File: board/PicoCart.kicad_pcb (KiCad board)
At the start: 2 copper layers, 99.8 x 99.5 mm, 29 parts, among them J1 MSX Bus (Odd-Even), J2 Micro_SD_Card, J3 UART, J4 DEBUG, J5 MSX Debug, J6 Pico Debug, J7 Ground Pins, J8 Ground Pins, J9 Edge Connector, U1 LD1117S33TR_SOT223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

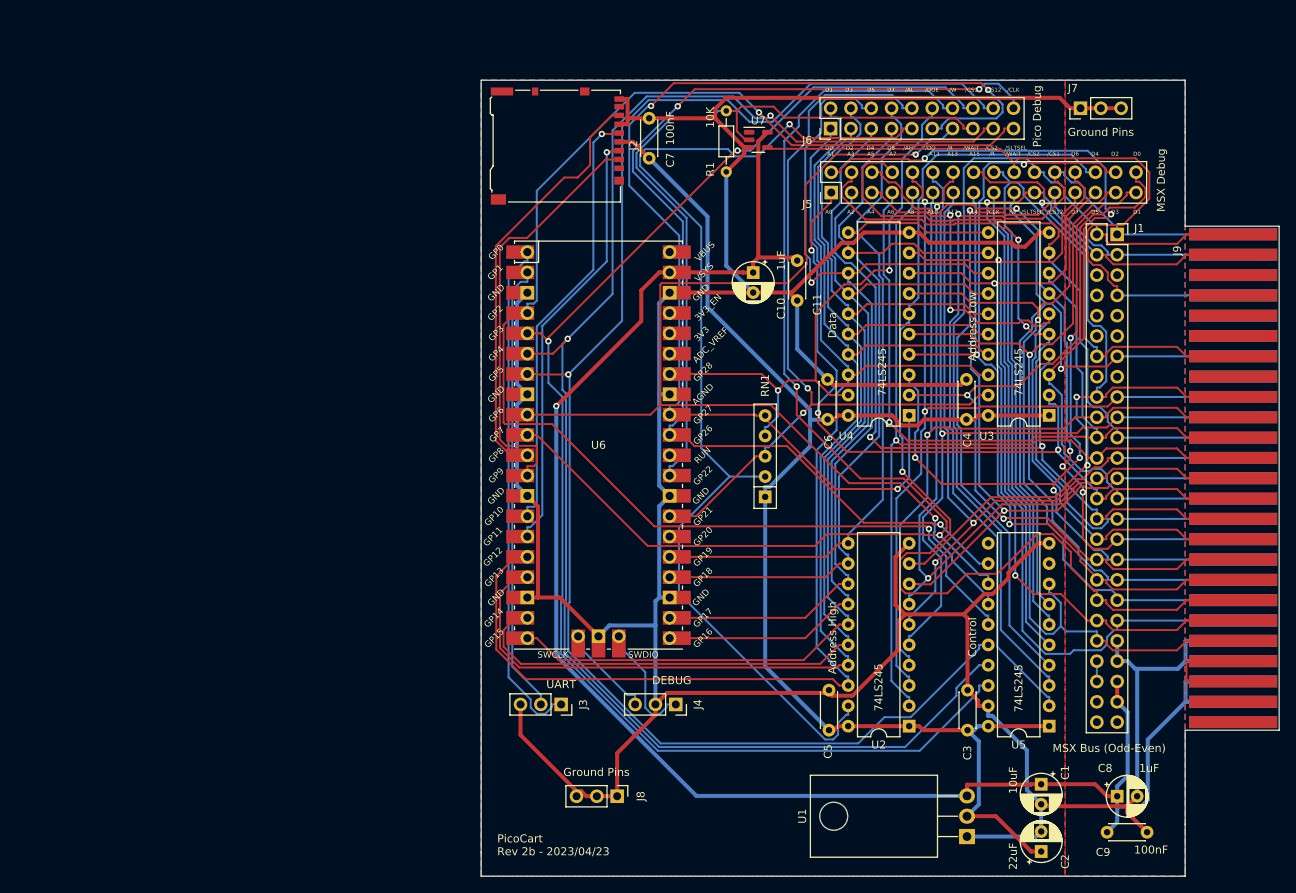
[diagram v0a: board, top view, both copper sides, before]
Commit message: Debug Board Design
Created a Debug board so that I can test the Main Pico logic against a
more controllable set of signals, rather than the MSX which provides a
very short window of usability
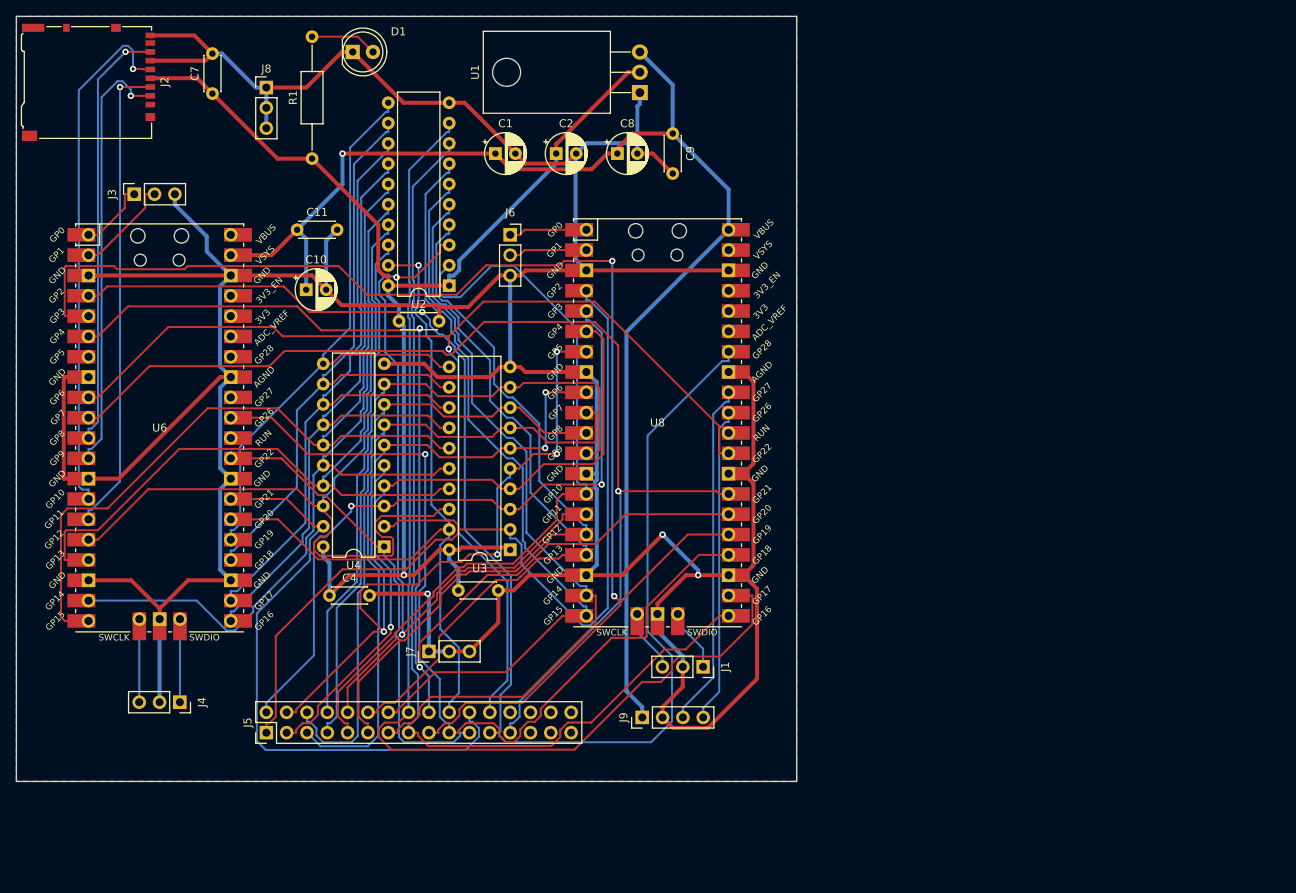
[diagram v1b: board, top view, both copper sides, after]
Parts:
- removed C6: 100nF, Capacitor_THT:C_Disc_D4.3mm_W1.9mm_P5.00mm
- removed RN1: 10K, Resistor_THT:R_Array_SIP5
- removed U5: 74LS245, Package_DIP:DIP-20_W7.62mm
- removed U7: SN74LV1T34DBV, Package_TO_SOT_SMD:SOT-23-5
- added D1: LED, LED_THT:LED_D5.0mm, F.Cu at (91.4, 37.5)
- added U8: Pico, Library:RPi_Pico_SMD_TH, F.Cu at (129.5, 83.8)
- J1: value MSX Bus (Odd-Even) -> D_DEBUG; footprint Connector_PinHeader_2.54mm:PinHeader_2x25_P2.54mm_Vertical -> Connector_PinSocket_2.54mm:PinSocket_1x03_P2.54mm_Vertical
- J6: value Pico Debug -> D_UART; footprint Connector_PinHeader_2.54mm:PinHeader_2x10_P2.54mm_Vertical -> Connector_PinSocket_2.54mm:PinSocket_1x03_P2.54mm_Vertical
- J9: value Edge Connector -> DEBUG_I2C; footprint Connector:MSX_Cartridge -> Connector_PinHeader_2.54mm:PinHeader_1x04_P2.54mm_Vertical
- R1: value 10K -> R_Small; footprint Resistor_THT:R_Axial_DIN0204_L3.6mm_D1.6mm_P7.62mm_Horizontal -> Resistor_THT:R_Axial_DIN0207_L6.3mm_D2.5mm_P15.24mm_Horizontal
- U6: footprint MCU_RaspberryPi_and_Boards:RPi_Pico_SMD_TH -> Library:RPi_Pico_SMD_TH
- moved C2 106.2 mm to (116.9, 50.2), turned to 0 degrees
- moved J7 106.0 mm to (101.0, 112.4)
- moved C1 104.3 mm to (109.3, 50.2), turned to 0 degrees
- moved C9 102.8 mm to (131.4, 47.7), turned to -90 degrees
- moved C8 101.8 mm to (124.5, 50.2)
- moved U1 101.6 mm to (127.3, 42.5)
- moved J8 98.9 mm to (80.6, 41.9), turned to 0 degrees
- moved J5 97.7 mm to (80.6, 122.6)
- moved J3 83.2 mm to (64.1, 55.2), turned to 90 degrees
- moved C4 82.6 mm to (88.5, 105.4), turned to 0 degrees
- moved J9 79.8 mm to (127.6, 120.7)
- moved U2 79.6 mm to (103.5, 66.7)
- moved J1 74.8 mm to (135.2, 114.3), turned to -90 degrees
- moved C5 74.2 mm to (97.2, 71.1), turned to 0 degrees
- moved U3 69.4 mm to (111.1, 99.7)
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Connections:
- J1 pad 1: /E_CS1 -> Net-(J1-Pin_1)
- J1 pad 2: /E_CS2 -> GND
- J1 pad 3: /E_CS12 -> Net-(J1-Pin_3)
- J5 pad 17: E_CLK -> /I_CS1
- J5 pad 18: /E_READ -> /I_CS2
- J5 pad 19: /E_WRITE -> /I_WAIT
- J5 pad 20: /WAIT -> /AOE
- J5 pad 21: /E_SLTSEL -> /DOUT
- J5 pad 22: /E_CS2 -> /DOE
- J5 pad 23: /E_CS12 -> /I_SLTSEL
- J5 pad 24: /E_CS1 -> /I_READ
- J5 pad 25: /E_D7 -> /I_WRITE
- J5 pad 26: /E_D6 -> unconnected-(J5-Pin_26-Pad26)
- J5 pad 27: /E_D5 -> unconnected-(J5-Pin_27-Pad27)
- J5 pad 28: /E_D4 -> unconnected-(J5-Pin_28-Pad28)
- J5 pad 29: /E_D3 -> unconnected-(J5-Pin_29-Pad29)
- J5 pad 30: /E_D2 -> unconnected-(J5-Pin_30-Pad30)
- J5 pad 31: /E_D1 -> unconnected-(J5-Pin_31-Pad31)
- J5 pad 32: /E_D0 -> unconnected-(J5-Pin_32-Pad32)
- J6 pad 1: /I_D0 -> D_UART_TX
- J6 pad 2: /I_D1 -> D_UART_RX
- J6 pad 3: /I_D2 -> GND
- J9 pad 1: /E_CS1 -> +5V
- J9 pad 2: /E_CS2 -> GND
- J9 pad 3: /E_CS12 -> SCL
- J9 pad 4: /E_SLTSEL -> SDA
- R1 pad 1: GND -> +3.3V
- R1 pad 2: /I_WAIT -> Net-(D1-A)
- U2 pad 19: /AHOE -> /AOE
- U3 pad 19: /ALOE -> /AOE
- U4 pad 2: /E_D0 -> /E_A0
- U4 pad 3: /E_D1 -> /E_A1
- U4 pad 4: /E_D2 -> /E_A2
- U4 pad 5: /E_D3 -> /E_A3
- U4 pad 6: /E_D4 -> /E_A4
- U4 pad 7: /E_D5 -> /E_A5
- U4 pad 8: /E_D6 -> /E_A6
- U4 pad 9: /E_D7 -> /E_A7
- U6 pad 26: /AHOE -> /AOE
- U6 pad 27: /ALOE -> /DOE
- U6 pad 29: /I_WAIT -> /DOUT
- U6 pad 31: I_CLK -> /I_WAIT
- U6 pad 32: /DOUT -> unconnected-(U6-GPIO27_ADC1-Pad32)_0
- U6 pad 34: /DOE -> unconnected-(U6-GPIO28_ADC2-Pad34)
- U6 pad 7: /I_CS12 -> unconnected-(U6-GPIO5-Pad7)
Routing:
- net /I_CS12: track 188.6 -> 0.00 mm, vias 1 -> 0
- net I_CLK: track 138.5 -> 0.00 mm, vias 3 -> 0
- net /AHOE: track 137.4 -> 0.00 mm, vias 1 -> 0
- net /E_D4: track 135.7 -> 0.00 mm, vias 1 -> 0
- net /E_CS1: track 112.6 -> 0.00 mm, vias 1 -> 0
- net /E_CS2: track 112.0 -> 0.00 mm
- net /E_D7: track 106.6 -> 0.00 mm, vias 1 -> 0
- net /E_READ: track 106.1 -> 0.00 mm
- net /E_D2: track 105.8 -> 0.00 mm, vias 3 -> 0
- net /E_D6: track 103.0 -> 0.00 mm, vias 2 -> 0
- net /E_D1: track 102.0 -> 0.00 mm, vias 4 -> 0
- net /E_CS12: track 101.4 -> 0.00 mm, vias 1 -> 0
- net /E_D0: track 101.1 -> 0.00 mm, vias 2 -> 0
- net /ALOE: track 100.4 -> 0.00 mm, vias 2 -> 0
- net /E_SLTSEL: track 95.1 -> 0.00 mm, vias 1 -> 0
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- added copper zone on F.Cu, net GND
- removed copper zone on F.Cu, net +3.3V
- removed copper zone on F.Cu, net +5V
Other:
- board size 99.8 x 99.5 mm -> 97.5 x 95.6 mm
- board text removed: "/AH"
- board text removed: "/AL"
- board text removed: "/CLK"
- board text removed: "/CS1"
- board text removed: "/CS12"
- board text removed: "/CS2"
- board text removed: "/DO"
- board text removed: "/DOE"
- board text removed: "/R"
- board text removed: "/SLTSEL"
- board text removed: "/W"
- board text removed: "/WAIT"
- board text removed: "A0"
- board text removed: "A1"
- board text removed: "A10"
- board text removed: "A11"
- board text removed: "A12"
- board text removed: "A13"
- board text removed: "A14"
- board text removed: "A15"
- board text removed: "A2"
- board text removed: "A3"
- board text removed: "A4"
- board text removed: "A5"
- board text removed: "A6"
- board text removed: "A7"
- board text removed: "A8"
- board text removed: "A9"
- board text removed: "Address High"
- board text removed: "Address Low"
- board text removed: "Control"
- board text removed: "D0"
- board text removed: "D1"
- board text removed: "D2"
- board text removed: "D3"
- board text removed: "D4"
- board text removed: "D5"
- board text removed: "D6"
- board text removed: "D7"
- board text removed: "Data"
- board text removed: "PicoCart Rev 2b - 2023/04/23"
